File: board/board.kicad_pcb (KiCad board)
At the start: 2 copper layers, 21 x 13 mm, 1 part

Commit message: initial
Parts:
- added C1: 100nF, Resistor_SMD:R_0603_1608Metric, F.Cu at (153.5, 91.5)
- added J1: 010_UART, on_edge:on_edge_2x05_device, F.Cu at (140.0, 96.5)
- added J2: Conn_01x03_Male, Connector_PinHeader_2.54mm:PinHeader_1x03_P2.54mm_Vertical, F.Cu at (159.0, 99.0)
- added R1: d.n.p, Resistor_SMD:R_0603_1608Metric, F.Cu at (146.5, 102.0)
- added R10: 10k, Resistor_SMD:R_0603_1608Metric, F.Cu at (156.0, 98.7)
- added R2: 0R, Resistor_SMD:R_0603_1608Metric, F.Cu at (145.8, 93.8)
- added R3: 0R, Resistor_SMD:R_0603_1608Metric, F.Cu at (145.8, 96.7)
- added R4: 2.2k, Resistor_SMD:R_0603_1608Metric, F.Cu at (149.0, 101.4)
- added R5: 2.2k, Resistor_SMD:R_0603_1608Metric, F.Cu at (150.5, 101.4)
- added R6: 2.2k, Resistor_SMD:R_0603_1608Metric, F.Cu at (152.0, 101.4)
- added R7: 2.2k, Resistor_SMD:R_0603_1608Metric, F.Cu at (153.5, 101.4)
- added R8: 10k, Resistor_SMD:R_0603_1608Metric, F.Cu at (156.0, 92.7)
- added R9: 120R, Resistor_SMD:R_0603_1608Metric, F.Cu at (156.0, 95.7)
- added U1: MAX485E, Package_SO:SO-8_3.9x4.9mm_P1.27mm, F.Cu at (150.5, 95.5)
- LOGO1: moved to B.Cu
- moved LOGO1 2.69 mm to (151.0, 96.5), turned to 180 degrees
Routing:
- net +3.3V: track 0.00 -> 29.7 mm, vias 0 -> 1
- net GND: track 0.00 -> 25.6 mm, vias 0 -> 2
- net /implementation/RX_EN: track 0.00 -> 18.2 mm
- net /implementation/RX: track 0.00 -> 15.7 mm
- net /implementation/TX: track 0.00 -> 10.0 mm
- net /implementation/TX_EN: track 0.00 -> 9.22 mm
- net /implementation/B: track 0.00 -> 7.67 mm
- net /implementation/A: track 0.00 -> 7.52 mm
- net Net-(J1-Pad5): track 0.00 -> 4.43 mm
- net Net-(J1-Pad6): track 0.00 -> 3.53 mm, vias 0 -> 1
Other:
- outline, holes or cut-outs redrawn

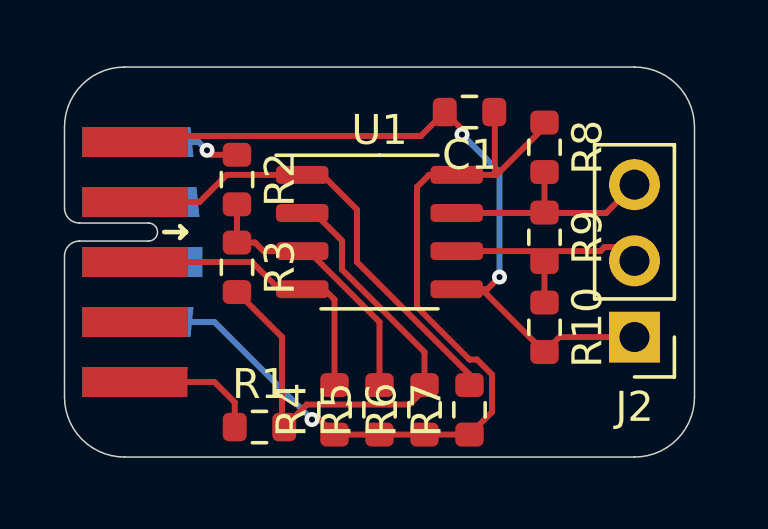
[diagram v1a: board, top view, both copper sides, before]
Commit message: changed supply to 5V and fixed up silkscreen
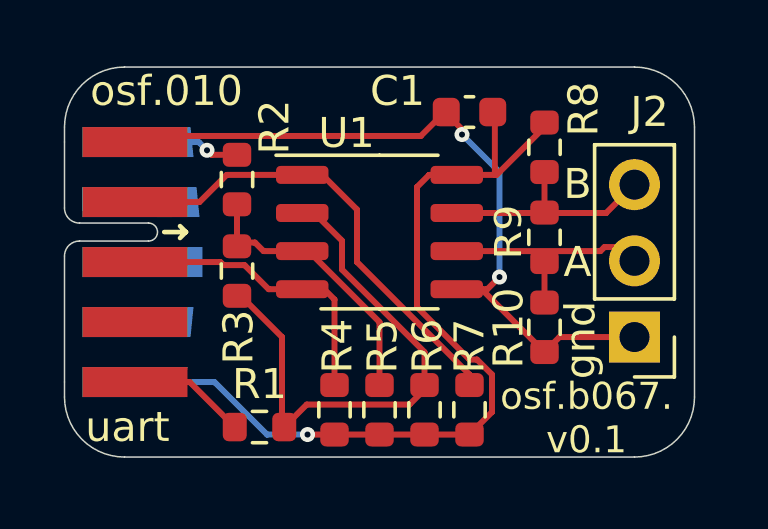
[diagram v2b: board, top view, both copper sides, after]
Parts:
- C1: footprint Resistor_SMD:R_0603_1608Metric -> Capacitor_SMD:C_0603_1608Metric
- moved R3 0.12 mm to (145.8, 96.8)
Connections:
- net /implementation/A renamed /max485/A
- net /implementation/B renamed /max485/B
- net /implementation/RX renamed /max485/RX
- net /implementation/RX_EN renamed /max485/RX_EN
- net /implementation/TX renamed /max485/TX
- net /implementation/TX_EN renamed /max485/TX_EN
- C1 pad 1: +3.3V -> +5V
- J1 pad 10: unconnected-(J1-Pad10) -> +5V
- J1 pad 9: +3.3V -> unconnected-(J1-Pad9)
- R4 pad 1: +3.3V -> +5V
- R5 pad 1: +3.3V -> +5V
- R6 pad 1: +3.3V -> +5V
- R7 pad 1: +3.3V -> +5V
- R8 pad 1: +3.3V -> +5V
- U1 pad 8: +3.3V -> +5V
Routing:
- net +3.3V: track 29.7 -> 0.00 mm, vias 1 -> 0
- net +5V: track 0.00 -> 29.0 mm, vias 0 -> 1
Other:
- board text added: "A"
- board text added: "B"
- board text added: "gnd"
- board text added: "osf.010"
- board text added: "osf.b067. v0.1"
- board text added: "osf.b067.v0.1"
- board text added: "uart"
